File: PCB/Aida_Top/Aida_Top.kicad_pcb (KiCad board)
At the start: 2 copper layers, 31 x 23.5 mm, 6 parts

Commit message: プレート作成中
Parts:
- H2: footprint Lib_Local:MountingHole_M2_Through-hole_tap_THC-0.8-2.0-2_minimal -> Lib_Local:MountingHole_M2_Through-hole_tap_THC-0.8-1.0-2_minimal
- H3: footprint Lib_Local:MountingHole_M2_Through-hole_tap_THC-0.8-2.0-2_minimal -> Lib_Local:MountingHole_2.2mm_M2_Pad_minimal
- moved H1 1.19 mm to (123.8, 36.3)
- moved H2 1.19 mm to (147.6, 52.4)
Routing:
- net COL_4_from_Mid: track 24.5 -> 25.3 mm
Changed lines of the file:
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@@
 		(embedded_fonts no)
 	)
-	(footprint "Lib_Local:MountingHole_M2_Through-hole_tap_THC-0.8-2.0-2_minimal"
+	(footprint "Lib_Local:MountingHole_2.2mm_M2_Pad_minimal"
 		(layer "F.Cu")
 		(at 139.303222 36.314073)
@@
 		(property "Datasheet" "~"
 			(at 0 0 0)
-			(unlocked yes)
 			(layer "F.Fab")
 			(hide yes)
@@
 		(property "Description" "Mounting Hole with connection"
 			(at 0 0 0)
-			(unlocked yes)
 			(layer "F.Fab")
 			(hide yes)
@@
 		(sheetname "/")
 		(sheetfile "Aida_Top.kicad_sch")
-		(attr exclude_from_bom)
+		(attr exclude_from_pos_files exclude_from_bom)
 		(fp_circle
 			(center 0 0)
-			(end 2.25 0)
+			(end 2.2 0)
 			(stroke
 				(width 0.15)
@@
 		(fp_circle
 			(center 0 0)
-			(end 2.8 0)
+			(end 2.45 0)
 			(stroke
 				(width 0.05)
@@
 			)
 		)
-		(pad "1" connect circle
+		(pad "1" thru_hole circle
 			(at 0 0)
 			(size 4.4 4.4)
-			(layers "F.Cu" "F.Mask")
-			(net 3 "COL_4_to_Base_via_Mid")
-			(pinfunction "1")
-			(pintype "input")
-		)
-		(pad "1" connect circle
-			(at 0 0)
-			(size 4.4 4.4)
-			(layers "B.Cu" "B.Mask")
-			(net 3 "COL_4_to_Base_via_Mid")
-			(pinfunction "1")
-			(pintype "input")
-		)
-		(pad "1" thru_hole circle
-			(at 0 0)
-			(size 5.5 5.5)
-			(drill 3.2)
+			(drill 2.2)
 			(layers "*.Cu" "*.Mask")
 			(remove_unused_layers no)
@@
 		)
 		(embedded_fonts no)
-		(model "${KIPRJMOD}/LIB_local/ThroughHole-Tap_THC-0.8-2.0-2-Fusion.step"
-			(offset
-				(xyz 0 0 0)
-			)
-			(scale
-				(xyz 1 1 1)
-			)
-			(rotate
-				(xyz 0 0 0)
-			)
-		)
 	)
 	(footprint "Lib_Local:Kailh_socket_ChocV2_small_#2pad_for_Reverse_no_hole"
@@
 	(footprint "Lib_Local:MountingHole_M2_Through-hole_tap_THC-0.8-1.0-2_minimal"
 		(layer "F.Cu")
-		(at 122.634458 36.314073)
+		(at 123.825084 36.314073)
 		(descr "Mounting Hole 2.2mm, M2")
 		(tags "mounting hole 2.2mm m2")
@@
 		)
 	)
-	(footprint "Lib_Local:MountingHole_M2_Through-hole_tap_THC-0.8-2.0-2_minimal"
+	(footprint "Lib_Local:MountingHole_M2_Through-hole_tap_THC-0.8-1.0-2_minimal"
 		(layer "F.Cu")
-		(at 147.637604 53.57815)
+		(at 147.637604 52.387524)
 		(descr "Mounting Hole 2.2mm, M2")
 		(tags "mounting hole 2.2mm m2")
@@
 		)
 		(embedded_fonts no)
-		(model "${KIPRJMOD}/LIB_local/ThroughHole-Tap_THC-0.8-2.0-2-Fusion.step"
+		(model "${KIPRJMOD}/LIB_local/ThroughHole-Tap_THC-0.8-1.0-2-Fusion.step"
 			(offset
 				(xyz 0 0 0)
@@
 	)
 	(gr_circle
-		(center 147.637604 53.57815)
-		(end 150.312354 53.57685)
-		(stroke
-			(width 0.1)
-			(type default)
-		)
-		(fill no)
-		(layer "Eco2.User")
-	)
-	(gr_circle
 		(center 127.3922 113.7026)
 		(end 130.06695 113.7013)
@@
 		(center 147.637604 84.534426)
 		(end 150.312354 84.533126)
-		(stroke
-			(width 0.1)
-			(type default)
-		)
-		(fill no)
-		(layer "Eco2.User")
-	)
-	(gr_circle
-		(center 122.634458 36.314073)
-		(end 125.309208 36.312773)
 		(stroke
 			(width 0.1)
@@
 	)
 	(gr_circle
-		(center 122.634458 36.314073)
-		(end 125.309208 36.312773)
+		(center 123.825084 36.314073)
+		(end 126.499834 36.312773)
 		(stroke
 			(width 0.1)
@@
 	)
 	(gr_circle
-		(center 122.634458 36.314073)
-		(end 125.309208 36.312773)
+		(center 123.825084 36.314073)
+		(end 126.499834 36.312773)
 		(stroke
 			(width 0.1)
@@
 	)
 	(gr_circle
-		(center 147.637604 53.57815)
-		(end 150.312354 53.57685)
+		(center 147.637604 52.387524)
+		(end 150.312354 52.386224)
 		(stroke
 			(width 0.1)
@@
 	)
 	(segment
-		(start 147.637604 54.173463)
-		(end 131.598463 54.173463)
-		(width 0.381)
-		(layer "B.Cu")
-		(net 2)
-	)
-	(segment
 		(start 131.598463 54.173463)
 		(end 131.3875 53.9625)
@@
 		(start 129.320696 51.5625)
 		(end 127.5625 51.5625)
+		(width 0.381)
+		(layer "B.Cu")
+		(net 2)
+	)
+	(segment
+		(start 146.062628 53.9625)
+		(end 131.3875 53.9625)
+		(width 0.381)
+		(layer "B.Cu")
+		(net 2)
+	)
+	(segment
+		(start 147.637604 52.387524)
+		(end 146.062628 53.9625)
 		(width 0.381)
 		(layer "B.Cu")
@@
 	)
 	(group ""
-		(members "099428c7-7952-4f7b-9cef-4940fc5f87ba" "17debefe-add8-47c9-a05a-0578d1d8277c"
-			"1c5d6183-0c96-4c5f-aa44-ac0a3ef4d39e" "2336c8a0-80f4-4dcf-933b-c718c9616f5a"
+		(members "17debefe-add8-47c9-a05a-0578d1d8277c" "1c5d6183-0c96-4c5f-aa44-ac0a3ef4d39e"
 			"25566046-2de5-4eb7-9a55-1bf68021d42f" "2ab9b7f4-02b2-4902-bd37-f68c16093bb7"
 			"317f203a-ee7a-4cc1-b884-9e615c7715ca" "348b522e-15ac-434f-a9ba-5069ddfb6eb2"

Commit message: プレート類調整中。LED位置検討中。
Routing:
- net GND: vias 0 -> 11
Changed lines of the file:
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@@
 		)
 		(embedded_fonts no)
-		(model "${KIPRJMOD}/locallib.pretty/kailh-socket-choc.stp"
+		(model "${KIPRJMOD}/Lib_Local/kailh-socket-choc.stp"
 			(offset
 				(xyz -2 -6.7 -3.5)
@@
 			)
 		)
-		(model "${KIPRJMOD}/locallib.pretty/Kailh_PG1353.STEP"
+		(model "${KIPRJMOD}/Lib_Local/Kailh_PG1353.STEP"
 			(offset
 				(xyz 0 0 2.6)
@@
 		)
 	)
+	(via
+		(at 149.4125 48.8125)
+		(size 0.6)
+		(drill 0.3)
+		(layers "F.Cu" "B.Cu")
+		(free yes)
+		(net 1)
+	)
+	(via
+		(at 135.2125 55.8125)
+		(size 0.6)
+		(drill 0.3)
+		(layers "F.Cu" "B.Cu")
+		(free yes)
+		(net 1)
+	)
+	(via
+		(at 120.6125 48.6125)
+		(size 0.6)
+		(drill 0.3)
+		(layers "F.Cu" "B.Cu")
+		(free yes)
+		(net 1)
+	)
+	(via
+		(at 120.6125 34.2125)
+		(size 0.6)
+		(drill 0.3)
+		(layers "F.Cu" "B.Cu")
+		(free yes)
+		(net 1)
+	)
+	(via
+		(at 149.4125 55.8125)
+		(size 0.6)
+		(drill 0.3)
+		(layers "F.Cu" "B.Cu")
+		(free yes)
+		(net 1)
+	)
+	(via
+		(at 149.0125 35.0125)
+		(size 0.6)
+		(drill 0.3)
+		(layers "F.Cu" "B.Cu")
+		(free yes)
+		(net 1)
+	)
+	(via
+		(at 136.6125 34.2125)
+		(size 0.6)
+		(drill 0.3)
+		(layers "F.Cu" "B.Cu")
+		(free yes)
+		(net 1)
+	)
+	(via
+		(at 138.4125 44.8125)
+		(size 0.6)
+		(drill 0.3)
+		(layers "F.Cu" "B.Cu")
+		(free yes)
+		(net 1)
+	)
+	(via
+		(at 142.0125 34.2125)
+		(size 0.6)
+		(drill 0.3)
+		(layers "F.Cu" "B.Cu")
+		(free yes)
+		(net 1)
+	)
+	(via
+		(at 135.2125 44.8125)
+		(size 0.6)
+		(drill 0.3)
+		(layers "F.Cu" "B.Cu")
+		(free yes)
+		(net 1)
+	)
+	(via
+		(at 120.6125 55.8125)
+		(size 0.6)
+		(drill 0.3)
+		(layers "F.Cu" "B.Cu")
+		(free yes)
+		(net 1)
+	)
 	(segment
 		(start 127.5625 51.5625)
@@
 	)
 	(segment
+		(start 135.33754 52.387524)
+		(end 133.762564 53.9625)
+		(width 0.381)
+		(layer "B.Cu")
+		(net 2)
+	)
+	(segment
 		(start 131.598463 54.173463)
 		(end 131.3875 53.9625)
@@
 	)
 	(segment
+		(start 133.762564 53.9625)
+		(end 131.3875 53.9625)
+		(width 0.381)
+		(layer "B.Cu")
+		(net 2)
+	)
+	(segment
 		(start 131.3875 53.9625)
 		(end 131.3875 53.629304)
@@
 	)
 	(segment
-		(start 146.062628 53.9625)
-		(end 131.3875 53.9625)
+		(start 147.637604 52.387524)
+		(end 135.33754 52.387524)
 		(width 0.381)
 		(layer "B.Cu")
-		(net 2)
-	)
-	(segment
-		(start 147.637604 52.387524)
-		(end 146.062628 53.9625)
-		(width 0.381)
-		(layer "B.Cu")

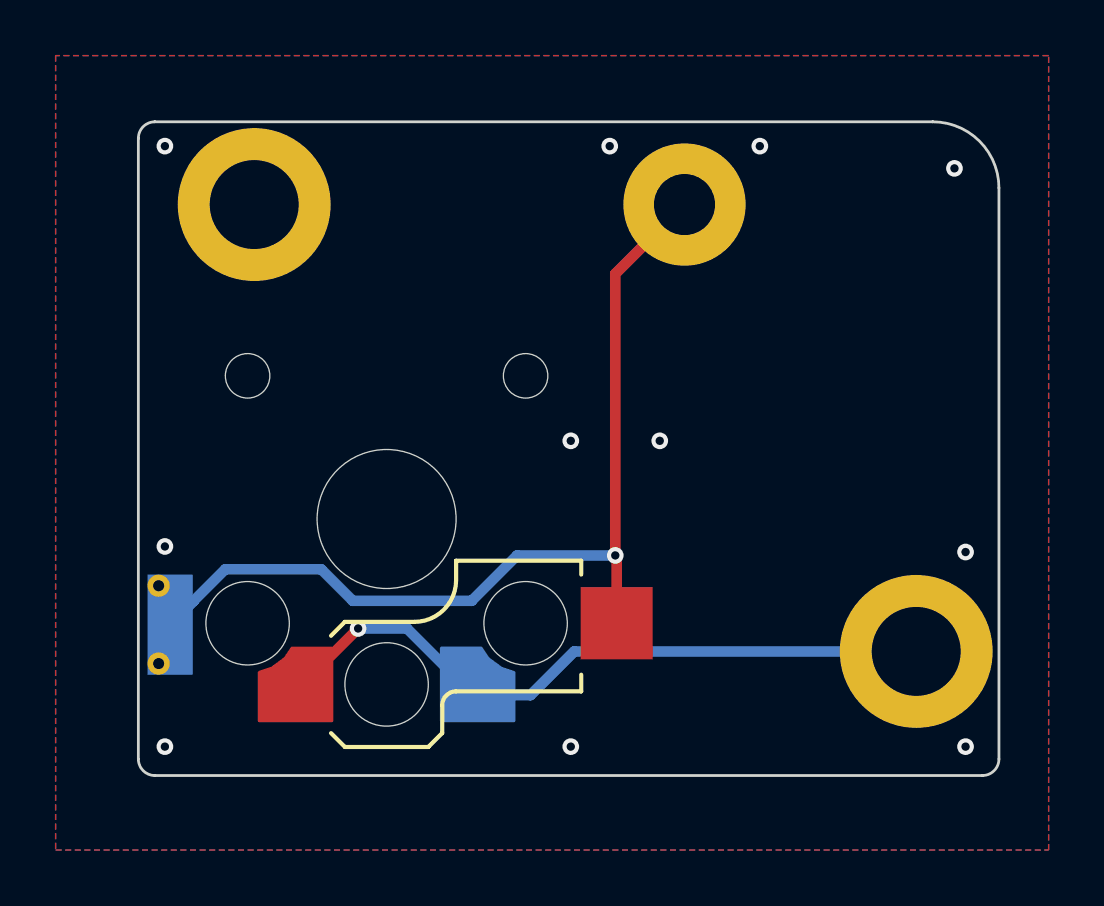
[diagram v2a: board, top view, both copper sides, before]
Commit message: テストポイントを追加、配置した。
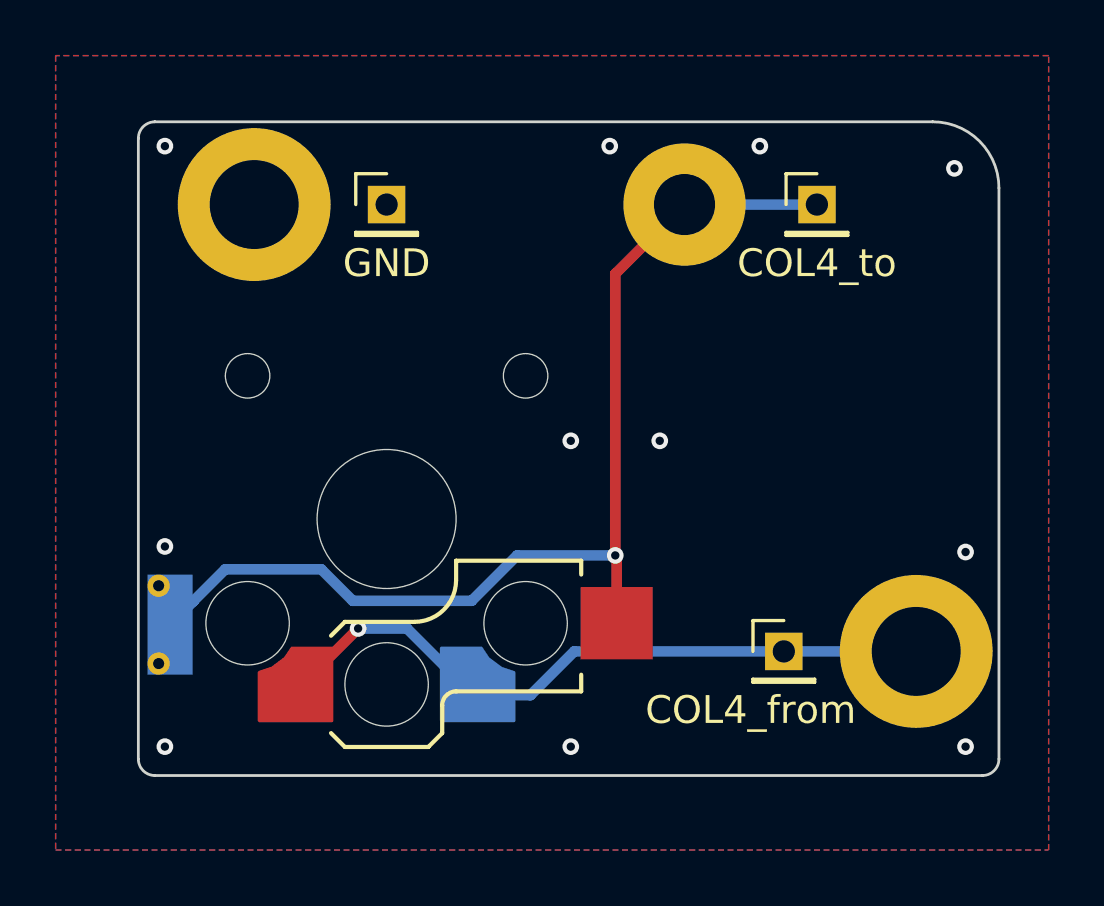
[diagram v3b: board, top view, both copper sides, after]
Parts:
- added TP1: GND, Connector_PinHeader_2.00mm:PinHeader_1x01_P2.00mm_Vertical, F.Cu at (128.6, 36.3)
- added TP2: COL4_from, Connector_PinHeader_2.00mm:PinHeader_1x01_P2.00mm_Vertical, F.Cu at (142.9, 52.4)
- added TP3: COL4_to, Connector_PinHeader_2.00mm:PinHeader_1x01_P2.00mm_Vertical, F.Cu at (144.1, 36.3)
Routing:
- net COL_4_to_Base_via_Mid: track 35.7 -> 40.4 mm

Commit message: 原点ガイドを追加。基板Mid_InsideのLED穴形状調整
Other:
- board text added: "Center Origin"
- board text added: "Grid Origin"
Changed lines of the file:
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@@
 		(layer "Edge.Cuts")
+	)
+	(gr_line
+		(start 150.01875 23.8125)
+		(end 154.78125 23.8125)
+		(stroke
+			(width 0.1)
+			(type default)
+		)
+		(layer "User.1")
+	)
+	(gr_circle
+		(center 23.8125 23.8125)
+		(end 25.003125 23.8125)
+		(stroke
+			(width 0.1)
+			(type default)
+		)
+		(fill no)
+		(layer "User.1")
+	)
+	(gr_line
+		(start 23.8125 21.43125)
+		(end 23.8125 26.19375)
+		(stroke
+			(width 0.1)
+			(type default)
+		)
+		(layer "User.1")
+	)
+	(gr_circle
+		(center 152.4 23.8125)
+		(end 153.590625 23.8125)
+		(stroke
+			(width 0.1)
+			(type default)
+		)
+		(fill no)
+		(layer "User.1")
+	)
+	(gr_line
+		(start 21.43125 23.8125)
+		(end 26.19375 23.8125)
+		(stroke
+			(width 0.1)
+			(type default)
+		)
+		(layer "User.1")
+	)
+	(gr_line
+		(start 152.4 21.43125)
+		(end 152.4 26.19375)
+		(stroke
+			(width 0.1)
+			(type default)
+		)
+		(layer "User.1")
 	)
 	(gr_text "Top PCB outline"
 		(at 156.865274 32.444558 0)
 		(layer "Eco1.User")
+		(effects
+			(font
+				(size 1 1)
+				(thickness 0.15)
+			)
+			(justify left bottom)
+		)
+	)
+	(gr_text "Grid Origin"
+		(at 20.240625 21.43125 0)
+		(layer "User.1")
+		(effects
+			(font
+				(size 1 1)
+				(thickness 0.15)
+			)
+			(justify left bottom)
+		)
+	)
+	(gr_text "Center Origin"
+		(at 148.828125 21.43125 0)
+		(layer "User.1")
 		(effects
 			(font
@@
 		)
 	)
+	(group ""
+		(members "2ffac422-b18f-483c-982b-707a96726745" "8f6b7b25-e383-42b6-abca-49e4382fde55"
+			"92e41497-a222-4a43-8584-2c072019dcea" "de23c7d7-404c-426f-826f-29133d7300d7"
+		)
+	)
+	(group ""
+		(members "4904038d-d6ed-4767-bf26-aab73137ac16" "9689cde1-cf7e-47a2-b36b-0af0e066dd8a"
+			"972ff840-2178-43ea-803a-caf217e92327" "ff16f92d-fbf4-4a07-8458-e46fd14acfc1"
+		)
+	)

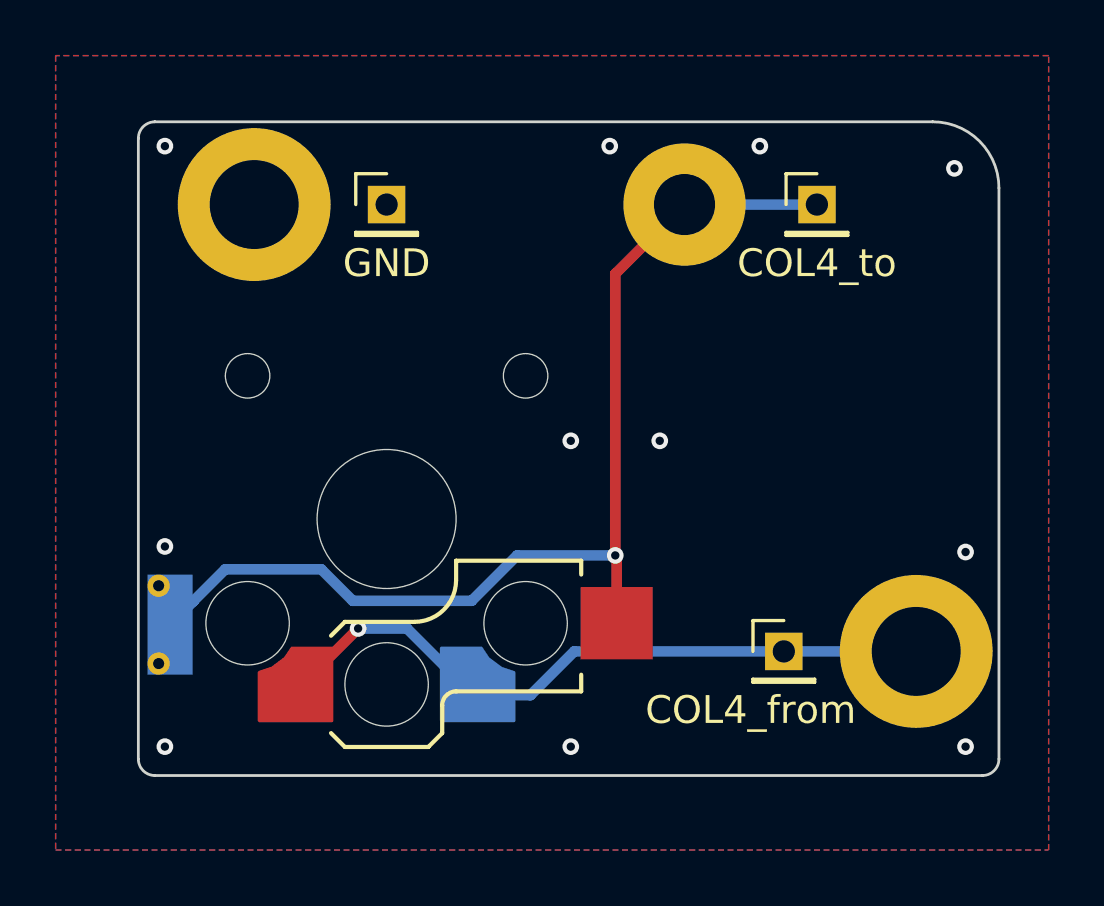
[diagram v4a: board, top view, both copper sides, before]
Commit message: 開発ナンバーと表裏を記載
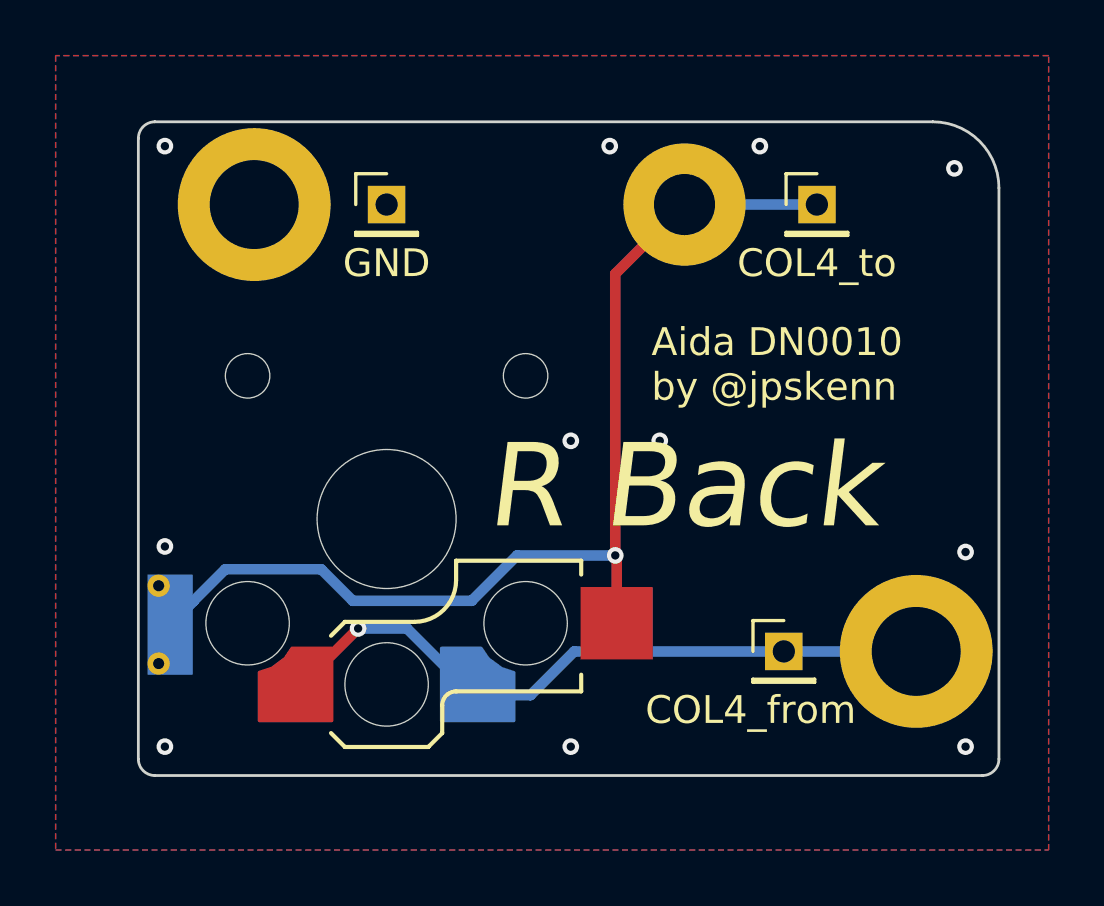
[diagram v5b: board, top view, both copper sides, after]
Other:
- board text added: "Aida DN0010 by @jpskenn"
- board text added: "L Back"
- board text added: "R Back"
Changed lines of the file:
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@@
 		(layer "User.1")
+	)
+	(gr_text "Aida DN0010\nby @jpskenn"
+		(at 138.112596 43.457829 0)
+		(layer "F.SilkS")
+		(effects
+			(font
+				(size 1 1)
+				(thickness 0.1)
+			)
+			(justify left bottom)
+		)
+	)
+	(gr_text "R Back"
+		(at 132.159466 48.220333 0)
+		(layer "F.SilkS" knockout)
+		(effects
+			(font
+				(size 3 3)
+				(thickness 0.375)
+				(italic yes)
+			)
+			(justify left bottom)
+		)
+	)
+	(gr_text "L Back"
+		(at 148.82823 48.220333 0)
+		(layer "B.SilkS" knockout)
+		(effects
+			(font
+				(size 3 3)
+				(thickness 0.375)
+				(italic yes)
+			)
+			(justify left bottom mirror)
+		)
 	)
 	(gr_text "Top PCB outline"
